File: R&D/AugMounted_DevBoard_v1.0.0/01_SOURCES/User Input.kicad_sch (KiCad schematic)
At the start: 4 parts, among them SW2 SW_EC12D1564404

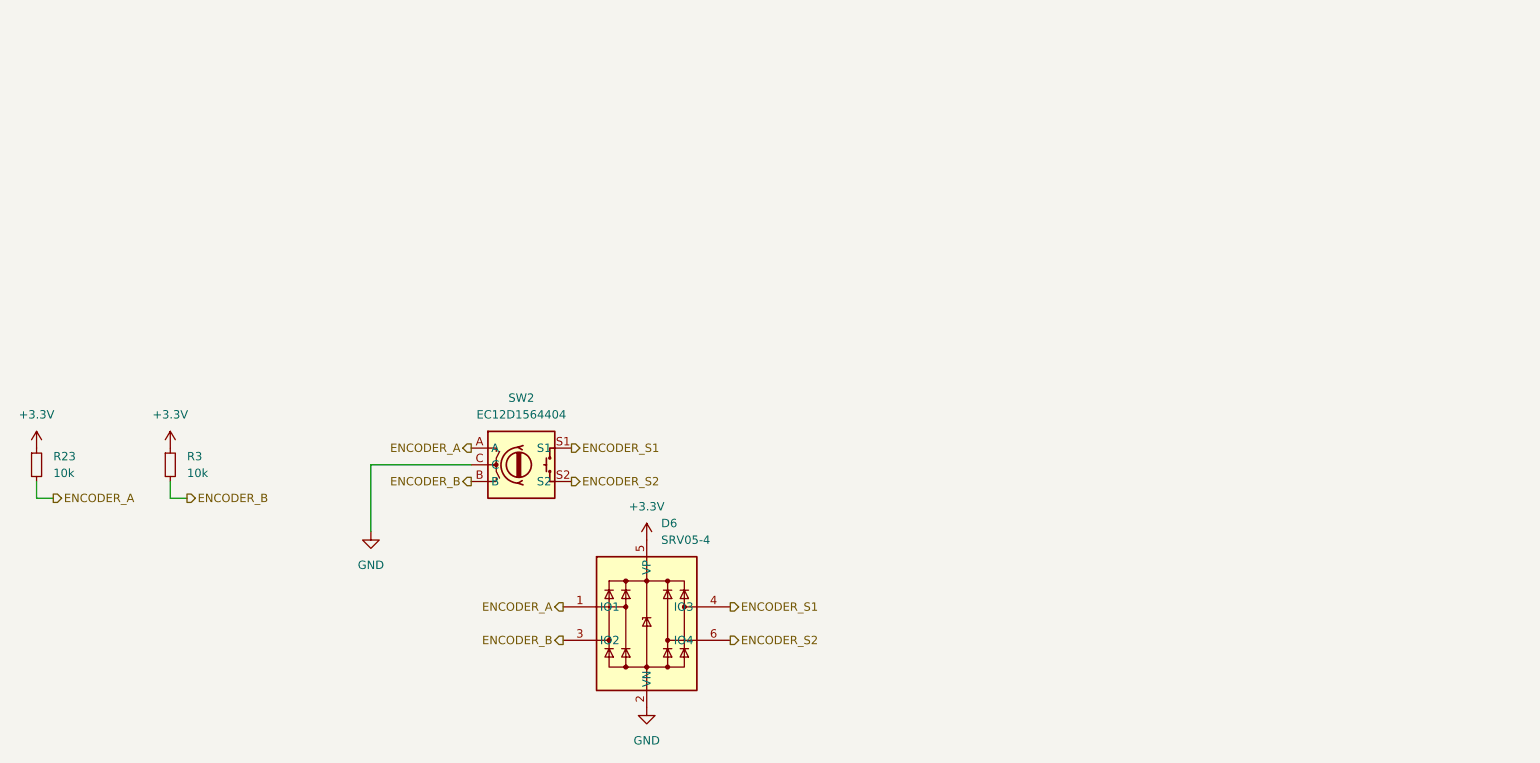
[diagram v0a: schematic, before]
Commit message: Schematic done
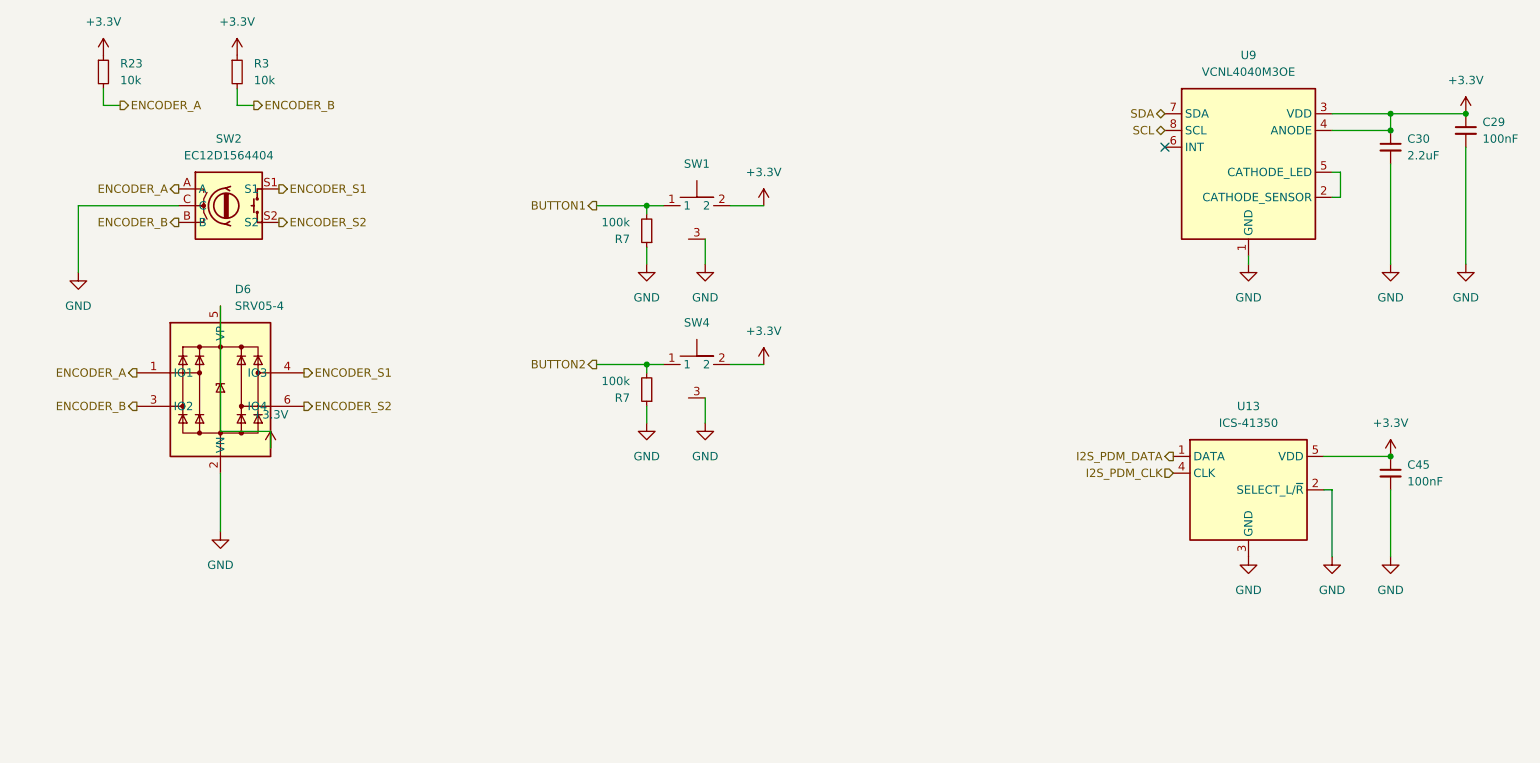
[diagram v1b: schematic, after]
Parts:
- added C29, C45: C_0603_100nF_100V_X7R_10%, .mounted-lib:C_0603_1608Metric, symbol .mounted-lib:C_0603_100nF_100V_X7R_10%
- added C30: C_0603_2.2uF_10V_X7R_10%, .mounted-lib:C_0603_1608Metric, symbol .mounted-lib:C_0603_2.2uF_10V_X7R_10%
- added R7 (x2): R_0603_100k_1%_0.1W, .mounted-lib:R_0603_1608Metric, symbol .mounted-lib:R_0603_100k_1%_0.1W
- added SW1, SW4: SW_SKRTLAE010, .mounted-lib:SW_SKRTLAE010, symbol .mounted-lib:SW_SKRTLAE010
- added U13: ICS‐41350, .mounted-lib:U_ICS-41350, symbol .mounted-lib:U_ICS‐41350
- added U9: U_VCNL4040M3OE, .mounted-lib:VCNL4040_4X2X1.1_VISHAY, symbol .mounted-lib:U_VCNL4040M3OE
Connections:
- net +3.3V: now also C29.1, C30.1, C45.1, SW1.2, SW4.2, U13.5 (VDD), U9.3 (VDD), U9.4 (ANODE)
- net GND: now also C29.2, C30.2, C45.2, R7.1, R7.1, SW1.3, SW4.3, U13.2 (SELECT_L/~{R}), U13.3 (GND), U9.1 (GND)
- new net: U9.2 (CATHODE_SENSOR), U9.5 (CATHODE_LED)
- new net BUTTON1: R7.2, SW1.1
- new net BUTTON2: R7.2, SW4.1
- new net I2S_PDM_CLK: U13.4 (CLK)
- new net I2S_PDM_DATA: U13.1 (DATA)
- new net SCL: U9.8 (SCL)
- new net SDA: U9.7 (SDA)
- no-connect marks 0 -> 1
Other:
- moved on the sheet: D6, R23, R3, SW2

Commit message: First revision of the layout
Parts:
- added C503: C_0603_100nF_100V_X7R_10%, .mounted-lib:C_0603_1608Metric, symbol .mounted-lib:C_0603_100nF_100V_X7R_10%
- added U?: LIS2DW12, Package_LGA:LGA-12_2x2mm_P0.5mm, symbol .mounted-lib:U_LIS2DW12
- renumbered C45 to C502, C30 to C?, C29 to C?, D6 to D501, R23 to R501, R3 to R502, R7 to R?, SW2 to SW501, SW1 to SW502, SW4 to SW503, U13 to U502, U9 to U?
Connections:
- net +3.3V: now also C503.1, U?.10 (VDDIO), U?.2 (CS), U?.9 (VDD)
- net GND: now also C503.2, U?.3 (SA0), U?.6 (GND), U?.7 (RES), U?.8 (GND)
- net SCL: now also U?.1 (SCL)
- net SDA: now also U?.4 (SDA)

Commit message: Changed layout to a banana shape
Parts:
- removed R? (x2): R_0603_100k_1%_0.1W, .mounted-lib:R_0603_1608Metric, symbol .mounted-lib:R_0603_100k_1%_0.1W
- removed SW501: SW_EC12D1564404, .mounted-lib:SW_EC12D1564404, symbol .mounted-lib:SW_EC12D1564404
- removed SW502, SW503: SW_SKRTLAE010, .mounted-lib:SW_SKRTLAE010, symbol .mounted-lib:SW_SKRTLAE010
- added D502: D_SRV05-4, .mounted-lib:SOT-23-6_TECH_PUBLIC, symbol .mounted-lib:D_SRV05-4
- added J501, J504: J_0788641001_PAD, .mounted-lib:J_788641001_PAD, symbol .mounted-lib:J_0788641001_PAD
- added J502, J503: J_0788641001, .mounted-lib:J_788641001, symbol .mounted-lib:J_0788641001
- added LED? (x3): LED_LTW-010DCG, .mounted-lib:LED_LTW-010DCG, symbol .mounted-lib:LED_LTW-010DCG
- added Q?: Q_BSS123WQ-7-F, .mounted-lib:SOT-323_SC-70_DIODES_INC, symbol .mounted-lib:Q_BSS123WQ-7-F
- added R501, R507: R_0603_0R_1%_0.1W, .mounted-lib:R_0603_1608Metric, symbol .mounted-lib:R_0603_0R_1%_0.1W
- added R? (x3): R_0603_100k_1%_0.1W, .mounted-lib:R_0603_1608Metric, symbol .mounted-lib:R_0603_100k_1%_0.1W
- added SW501: SW_SKRTLAE010, .mounted-lib:SW_SKRTLAE010, symbol .mounted-lib:SW_SKRTLAE010
- renumbered R501 to R503
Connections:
- net +3.3V: now also D502.5 (VP), J501.2, LED?.2 (A), LED?.2 (A), LED?.2 (A), R?.1, R?.1
- net BUTTON1: now also D502.6 (IO4), J501.5, R?.2
- net BUTTON2: now also D502.4 (IO3), J501.4, R?.2
- net ENCODER_A: now also J504.5
- net ENCODER_B: now also J504.4
- net ENCODER_S1: now also D501.6 (IO4), J504.1, SW501.2; no longer D501.4 (IO3)
- net ENCODER_S2: now also D501.4 (IO3), J504.6, SW501.1; no longer D501.6 (IO4)
- net GND: now also D502.2 (VN), J501.3, J501.6, J504.3, Q?.2 (S), R?.2, SW501.3
- new net: LED?.1 (K), LED?.1 (K), LED?.1 (K), R507.1
- new net: J502.1, J502.6
- new net: Q?.3 (D), R507.2
- new net: J501.1, R501.2
- new net BUTTON1_HMI_BOARD: J502.5
- new net BUTTON2_HMI_BOARD: J502.4
- new net ENCODER_A_HMI_BOARD: J503.5
- new net ENCODER_B_HMI_BOARD: J503.4
- new net ENCODER_S1_HMI_BOARD: J503.1
- new net ENCODER_S2_HMI_BOARD: J503.6
- new net GND_HMI_BOARD: J502.3, J503.3
- new net LEDS_ENABLE: Q?.1 (G), R?.1
- new net PLUG_DETECTION: D502.1 (IO1), R501.1
- new net VBUS: J504.2
- no-connect marks 1 -> 4
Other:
- added sheet HMI_BOARD (HMI_BOARD.kicad_sch)
- note added: "HMI BOARD"
- moved on the sheet: D501, R502, R503

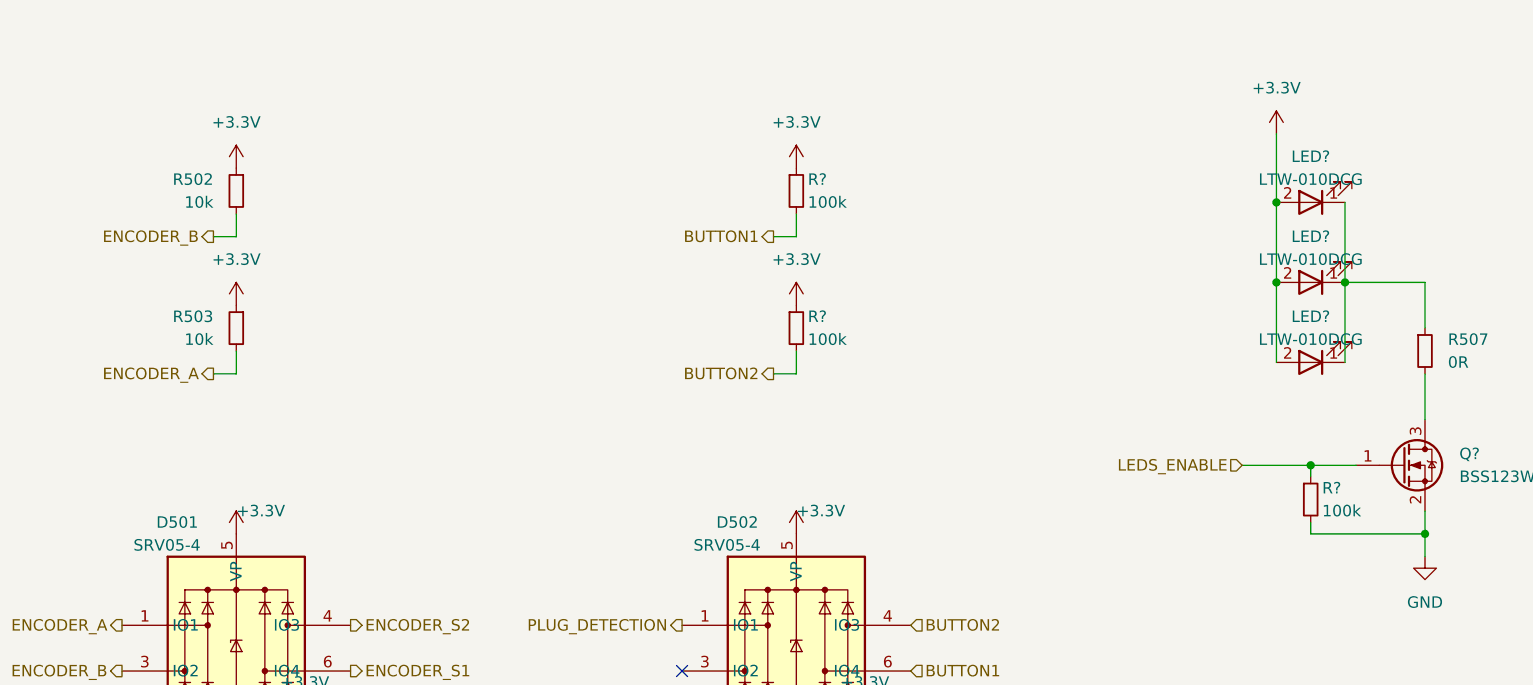
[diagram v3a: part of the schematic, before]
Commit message: Changed layout + all passive to 0402
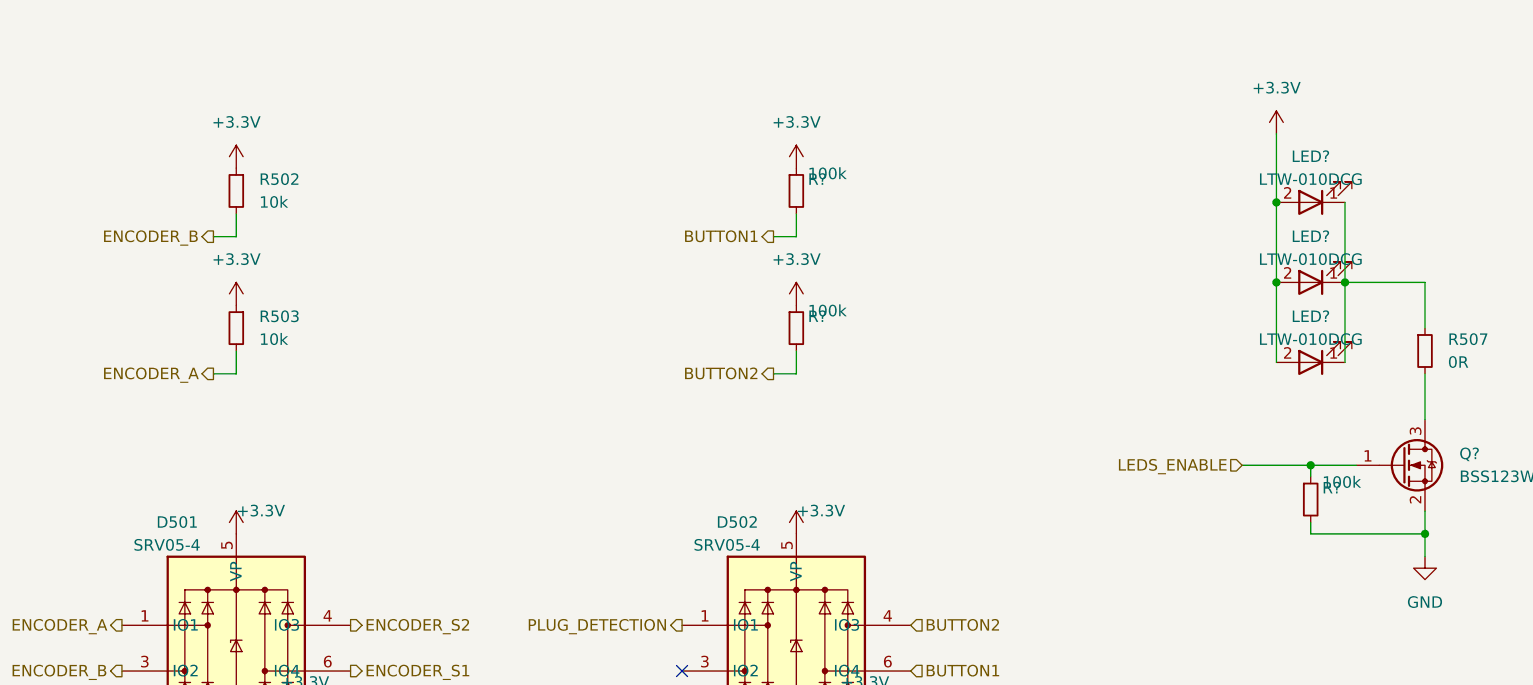
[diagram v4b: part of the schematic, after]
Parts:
- C502, C503, C?: footprint .mounted-lib:C_0603_1608Metric -> .mounted-lib:C_0402_1005Metric; symbol .mounted-lib:C_0603_100nF_100V_X7R_10% -> .mounted-lib:C_0402_100nF_50V_X7R_10%; MaxHeight_mm 0.8mm -> 0.5mm; Voltage 100V -> 50V
- R501, R507: value R_0603_0R_1%_0.1W -> R_0402_0R_1%_0.06W; footprint .mounted-lib:R_0603_1608Metric -> .mounted-lib:R_0402_1005Metric; symbol .mounted-lib:R_0603_0R_1%_0.1W -> .mounted-lib:R_0402_0R_1%_0.06W; MaxHeight_mm 0.55 -> 0.35MM; Package R0603 -> R0402; Power_W 0.1W -> 0.06W
- R502, R503: footprint .mounted-lib:R_0603_1608Metric -> .mounted-lib:R_0402_1005Metric; symbol .mounted-lib:R_0603_10k_1%_0.1W -> .mounted-lib:R_0402_10k_1%_0.06W; MaxHeight_mm 0.55mm -> 0.35mm; Package R0603 -> R0402; Power_W 0.1W -> 0.06W
- R? (x3): value R_0603_100k_1%_0.1W -> R_0402_100k_1%_0.06W; footprint .mounted-lib:R_0603_1608Metric -> .mounted-lib:R_0402_1005Metric; symbol .mounted-lib:R_0603_100k_1%_0.1W -> .mounted-lib:R_0402_100k_1%_0.06W; CMP_ID 50 -> 1068; MaxHeight_mm 0.55mm -> 0.35mm; Package R0603 -> R0402; Power_W 0.1W -> 0.06W; _Created GCE 2022-05-12 -> JCN 2023-11-24
